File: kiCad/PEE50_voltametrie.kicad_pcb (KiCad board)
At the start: 2 copper layers, 53 parts, among them IC1 MIC5219-3.3YM5-TR, IC2 TPS7A2045PDBVR, IC3 TMUX1109PWR, IC5 ADS1113IDGSR, IC6 DAC80501MDGSR, IC7 LMP7702MA_NOPB, IC8 DS18B20+, J1 2201778-1, J2 USB_B_Micro, J4 Conn_02x03_Odd_Even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

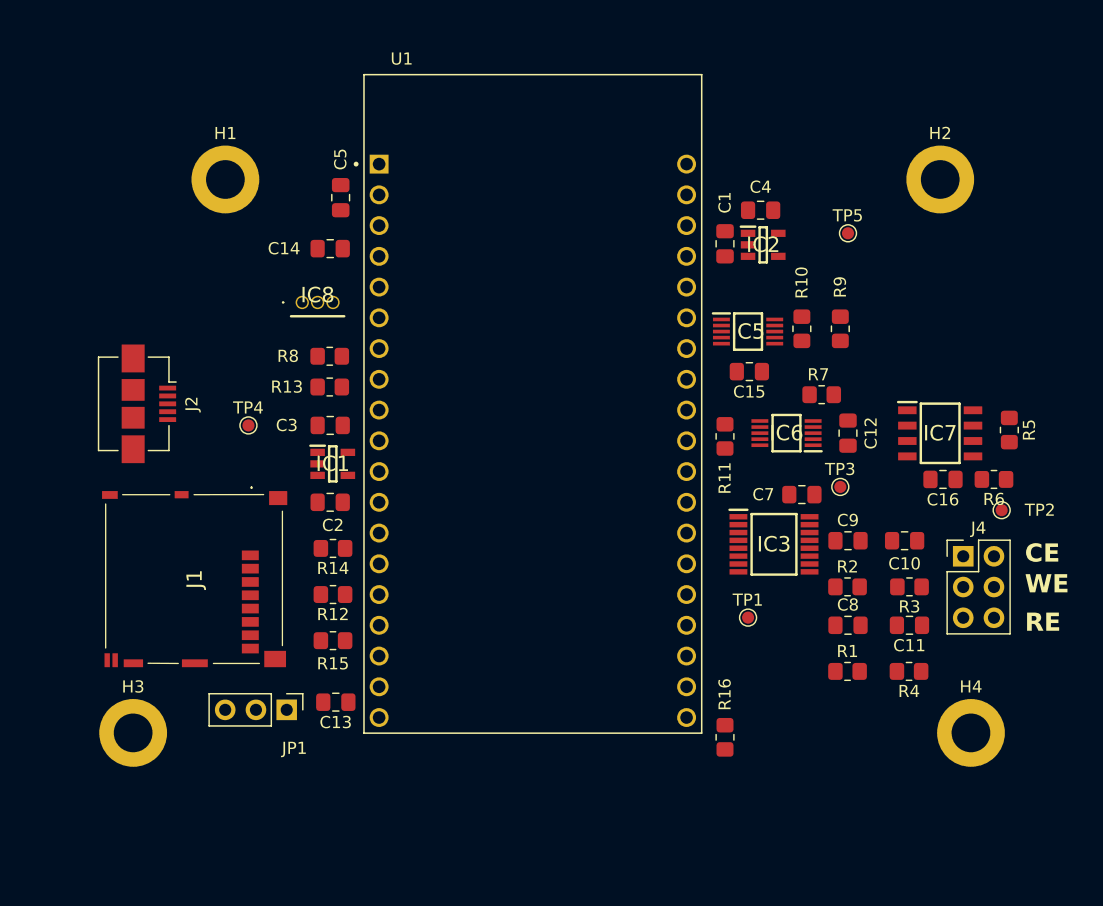
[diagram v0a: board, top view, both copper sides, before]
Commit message: Version 2 kicad files
Before traces are added
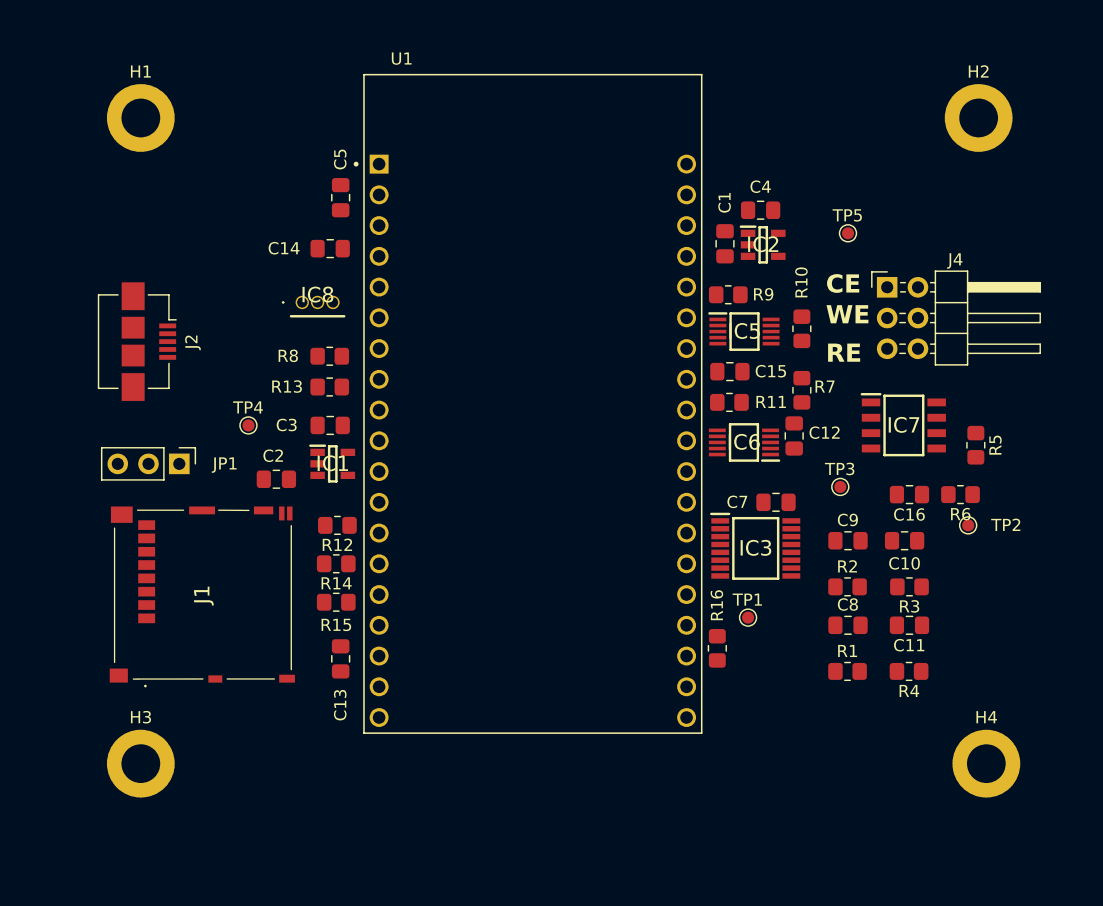
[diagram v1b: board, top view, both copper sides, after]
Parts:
- J4: footprint Connector_PinHeader_2.54mm:PinHeader_2x03_P2.54mm_Vertical -> Connector_PinHeader_2.54mm:PinHeader_2x03_P2.54mm_Horizontal
- moved J4 23.1 mm to (202.0, 87.0)
- moved JP1 22.2 mm to (143.5, 101.6)
- moved R9 9.67 mm to (188.9, 87.6), turned to 180 degrees
- moved H1 8.64 mm to (140.3, 73.0)
- moved R16 7.38 mm to (188.0, 116.8)
- moved H2 5.99 mm to (209.6, 73.0)
- moved R12 5.73 mm to (156.6, 106.7)
- moved J2 5.14 mm to (141.0, 91.5)
- moved C2 4.84 mm to (151.5, 102.9)
- moved C12 4.45 mm to (194.3, 99.3)
- moved C13 3.60 mm to (156.8, 117.7), turned to -90 degrees
- moved IC6 3.60 mm to (190.2, 99.8)
- moved R15 3.19 mm to (156.5, 113.0)
- moved IC7 3.07 mm to (203.4, 98.4)
- moved R5 3.04 mm to (209.3, 100.1)
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
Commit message: Version 3 kicad
Withoud 3.3V regulator not needed because of devkit
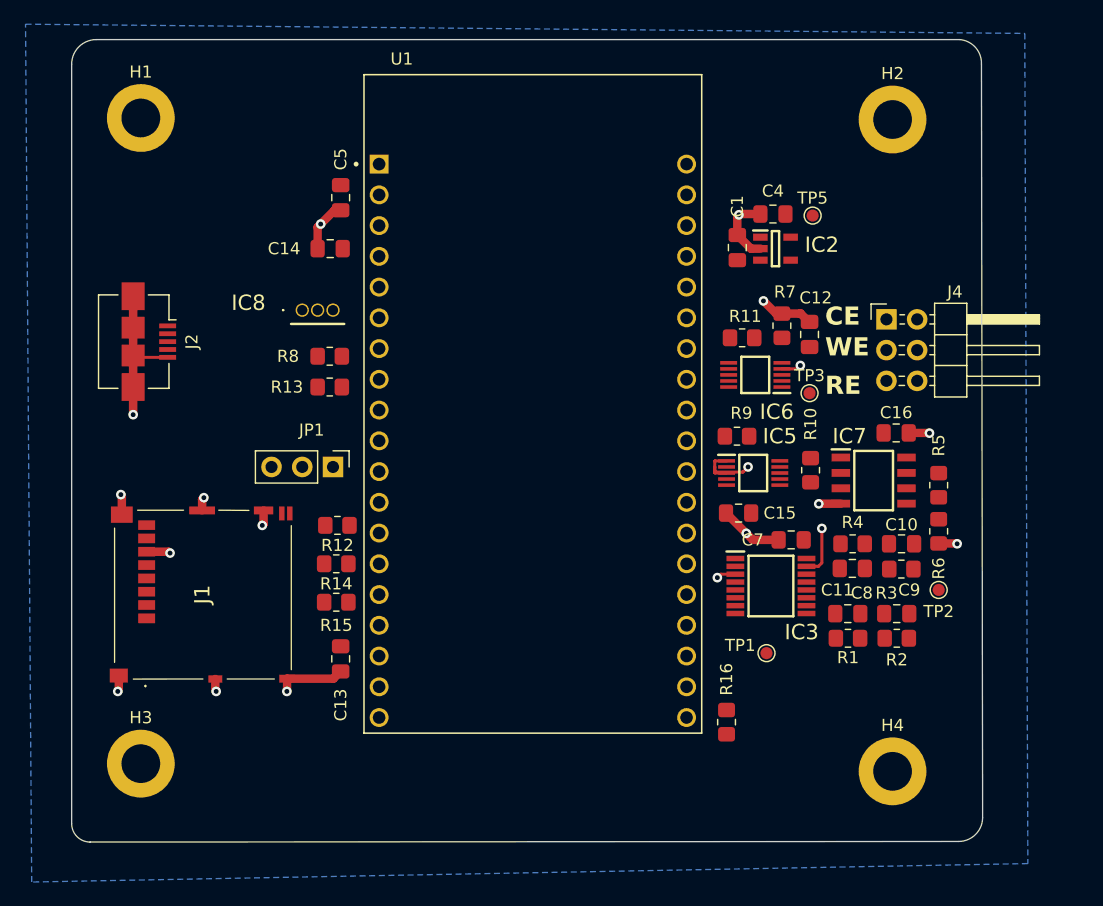
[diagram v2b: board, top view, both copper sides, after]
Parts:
- removed C2: 470p, Capacitor_SMD:C_0805_2012Metric_Pad1.18x1.45mm_HandSolder
- removed C3: 2.2u, Capacitor_SMD:C_0805_2012Metric_Pad1.18x1.45mm_HandSolder
- removed IC1: MIC5219-3.3YM5-TR, MIC5219-3.3YM5-TR:SOT95P280X145-5N
- removed TP4: TestPoint, TestPoint:TestPoint_Pad_D1.0mm
- moved JP1 12.7 mm to (156.2, 101.9)
- moved C15 11.7 mm to (189.7, 105.7)
- moved IC5 11.7 mm to (190.9, 102.4)
- moved R10 11.7 mm to (195.7, 102.1)
- moved R9 11.7 mm to (189.6, 99.3)
- moved R4 11.5 mm to (199.1, 108.2), turned to 0 degrees
- moved C12 8.48 mm to (195.6, 90.9)
- moved TP3 8.15 mm to (195.6, 95.8)
- moved H4 7.77 mm to (202.4, 127.0)
- moved C9 7.25 mm to (202.8, 114.0), turned to 180 degrees
- moved H2 7.11 mm to (202.4, 73.2)
- moved C11 6.66 mm to (199.1, 110.2), turned to 0 degrees
- moved R16 6.14 mm to (188.7, 122.9)
- moved R2 5.88 mm to (202.8, 116.0), turned to 180 degrees
- moved TP2 5.86 mm to (206.2, 112.0)
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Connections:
- U1 pad J2-14: unconnected-(U1-GND1-PadJ2-14) -> GND
- U1 pad J2-19: unconnected-(U1-EXT_5V-PadJ2-19) -> 5V
- U1 pad J3-1: unconnected-(U1-GND3-PadJ3-1) -> GND
- U1 pad J3-7: unconnected-(U1-GND2-PadJ3-7) -> GND
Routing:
- net GND: track 0.00 -> 65.7 mm, vias 0 -> 19
- added copper zone on B.Cu, net GND
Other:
- board outline added: 75.3 x 66.3 mm

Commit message: layout aangepast
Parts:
- moved R9 16.3 mm to (188.8, 83.0), turned to 90 degrees
- moved R10 15.3 mm to (188.8, 88.5), turned to -90 degrees
- moved TP2 13.1 mm to (193.2, 111.2)
- moved C12 8.33 mm to (198.3, 98.8)
- moved TP3 7.97 mm to (189.3, 100.7)
- moved IC3 7.89 mm to (198.7, 106.9)
- moved R16 6.95 mm to (188.2, 116.0)
- moved C11 6.57 mm to (204.8, 107.0)
- moved R4 6.50 mm to (204.8, 105.0)
- moved R7 6.45 mm to (196.6, 95.7), turned to 0 degrees
- moved TP1 6.09 mm to (191.2, 111.2)
- moved C7 6.03 mm to (197.6, 103.0)
- moved C16 5.49 mm to (208.2, 98.5), turned to 90 degrees
- moved R1 5.29 mm to (195.6, 111.8), turned to -90 degrees
- moved R2 5.28 mm to (199.7, 111.8), turned to -90 degrees
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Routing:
- net 4.5V: track 0.00 -> 158.7 mm, vias 0 -> 2
- net 5V: track 0.00 -> 101.9 mm
- net Net-(J1-VDD): track 0.00 -> 81.4 mm
- net GND: track 65.7 -> 0.00 mm, vias 19 -> 0
- net CS1: track 0.00 -> 60.9 mm
- net We: track 0.00 -> 36.0 mm
- net SCL1: track 0.00 -> 35.3 mm
- net MVref: track 0.00 -> 30.5 mm
- net 3.3V: track 0.00 -> 28.1 mm
- net CLCK1: track 0.00 -> 25.4 mm
- net SDA1: track 0.00 -> 25.3 mm
- net SDA2: track 0.00 -> 24.7 mm
- net MOSI1: track 0.00 -> 20.4 mm
- net MISO1: track 0.00 -> 19.9 mm
- net S4: track 0.00 -> 18.4 mm
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- added copper zone on F.Cu, net GND

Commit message: tested code
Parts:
- removed R13: 4k7, Resistor_SMD:R_0805_2012Metric_Pad1.20x1.40mm_HandSolder
- moved R16 31.1 mm to (157.2, 118.0), turned to -90 degrees
- moved R14 5.66 mm to (157.2, 104.2), turned to 90 degrees
- moved C13 2.50 mm to (155.2, 115.8)
- moved JP1 1.86 mm to (155.3, 100.2)
- moved R12 1.39 mm to (155.2, 106.2), turned to 90 degrees
- moved R15 0.90 mm to (157.2, 113.5), turned to 90 degrees
- moved R8 0.46 mm to (156.0, 92.2), turned to 0 degrees
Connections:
- C14 pad 1: 3.3V -> 4.5V
- IC8 pad 2: Net-(IC8-DQ) -> temp
- IC8 pad 3: 3.3V -> 4.5V
- R8 pad 2: Net-(IC8-DQ) -> 4.5V
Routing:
- net 4.5V: track 158.7 -> 194.9 mm
- net Net-(J1-VDD): track 81.4 -> 46.9 mm
- net 5V: track 101.9 -> 132.8 mm
- net CS1: track 60.9 -> 48.7 mm
- net S4: track 18.4 -> 10.9 mm
- net ChipSelect: track 17.7 -> 10.6 mm
- net SCL1: track 35.3 -> 41.7 mm
- net Net-(IC8-DQ): track 3.81 -> 0.00 mm
- net temp: track 5.88 -> 9.19 mm
- net CLCK1: track 25.4 -> 27.6 mm
- net MOSI1: track 20.4 -> 22.2 mm, vias 0 -> 1
- net SDA2: track 24.7 -> 23.7 mm
- net Net-(IC6-SPI2C): track 3.17 -> 2.21 mm
- net S1: track 10.5 -> 9.61 mm
- net MVref: track 30.5 -> 29.6 mm
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
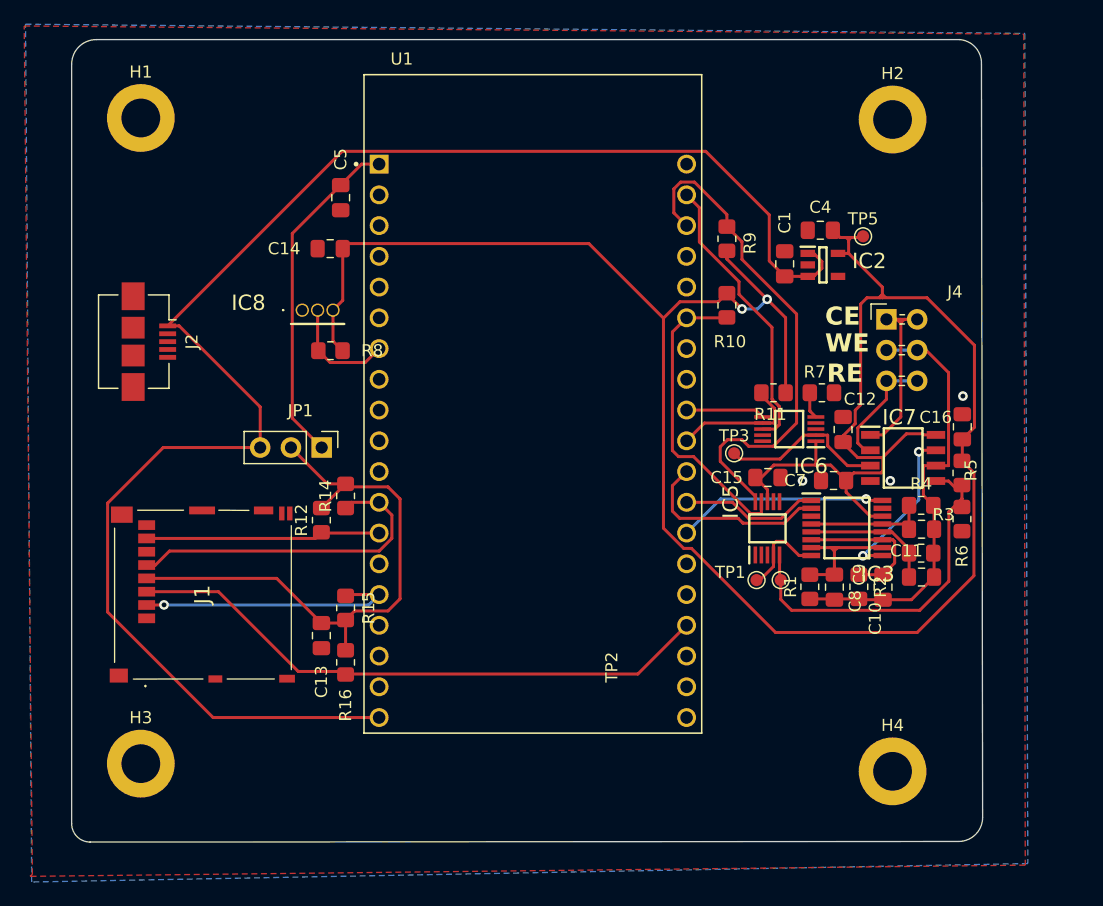
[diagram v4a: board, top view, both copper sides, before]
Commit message: SPI pin changes
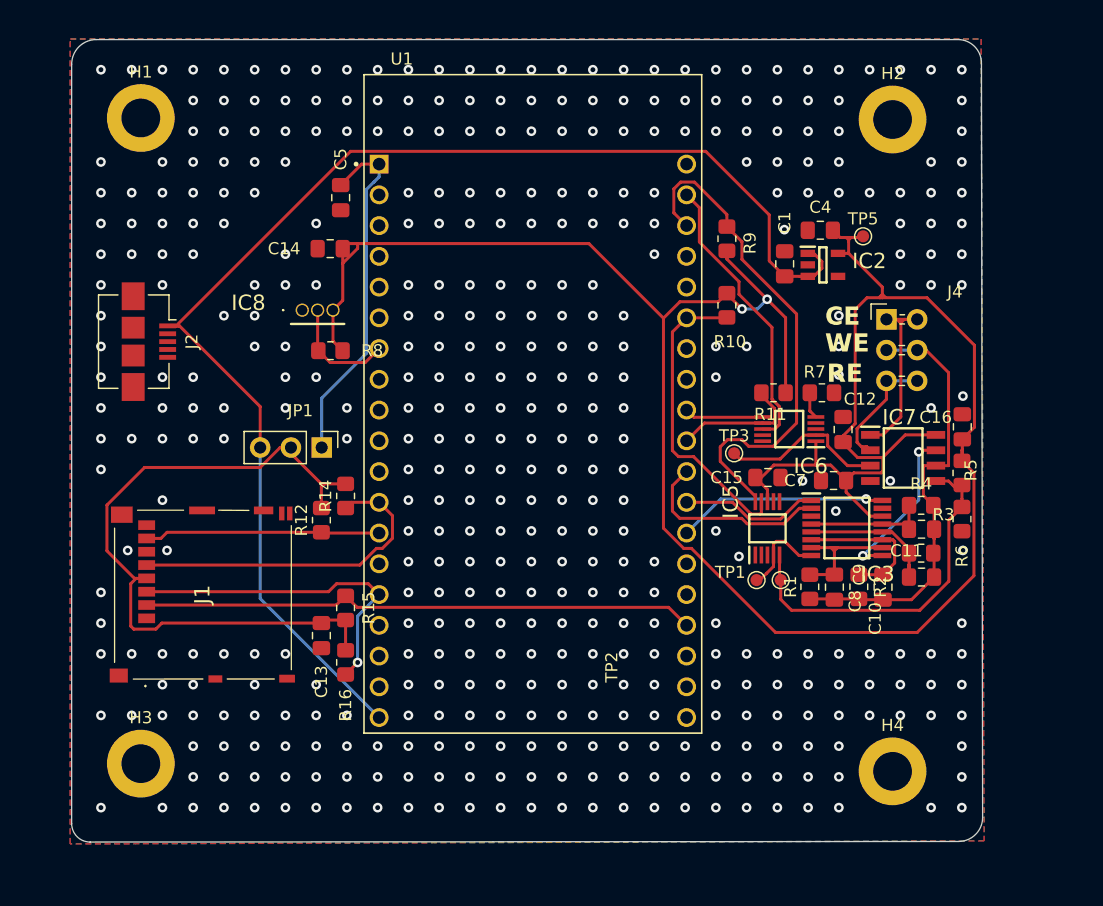
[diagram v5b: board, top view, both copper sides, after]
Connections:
- net CLCK1 renamed SCK2
- net MISO1 renamed MISO2
- net SCL2 renamed SCK1
- IC6 pad 7: ChipSelect -> CS1
- IC6 pad 8: SDA2 -> MOSI1
- J1 pad 2: MOSI1 -> CS2
- J1 pad 3: CS1 -> MOSI2
- R11 pad 2: ChipSelect -> CS1
- R15 pad 2: MOSI1 -> CS2
- R16 pad 2: CS1 -> MOSI2
- U1 pad J2-15: MOSI1 -> MOSI2
- U1 pad J3-10: ChipSelect -> CS1
- U1 pad J3-16: CS1 -> CS2
- U1 pad J3-2: SDA2 -> MOSI1
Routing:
- net CS2: track 0.00 -> 45.9 mm
- net CS1: track 48.7 -> 10.6 mm
- net MOSI2: track 0.00 -> 27.6 mm, vias 0 -> 1
- net 5V: track 132.8 -> 108.6 mm
- net SDA2: track 23.7 -> 0.00 mm
- net ChipSelect: track 10.6 -> 0.00 mm
- net Net-(J1-VDD): track 46.9 -> 57.0 mm
- net 4.5V: track 194.9 -> 197.5 mm
- net MOSI1: track 22.2 -> 23.7 mm, vias 1 -> 0
- net 3.3V: track 28.2 -> 29.3 mm
- net Re: track 9.50 -> 10.4 mm
- net MVref: track 29.6 -> 29.1 mm
- net S2: track 10.6 -> 11.1 mm
- net GND: vias 3 -> 434

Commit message: final pcb update
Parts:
- moved H2 2.81 mm to (205.0, 72.0)
- moved H4 2.56 mm to (205.0, 127.0)
- moved H1 1.08 mm to (140.0, 72.0)
- moved H3 0.72 mm to (140.0, 127.0)
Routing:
- net GND: vias 434 -> 432
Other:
- board size 75.3 x 66.3 mm -> 75 x 65 mm
- board text added: "PEE50 Juni 2023 Voltammetrie"
- board text removed: "PEE50 Mei 2023 Voltametrie"
